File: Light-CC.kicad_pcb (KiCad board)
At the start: 2 copper layers, 69 x 36 mm, 69 parts, among them J1 Conn_01x02_Pin, J2 Conn_01x02_Pin, J3 Conn_01x02_Pin, J4 Conn_01x03_Male, J5 USB_C_Receptacle_USB2.0, Q1 BS870, Q2 STD7NK40Z, Q3 BS870, Q4 BC547, Q5 BC547, Q6 BC547, U1 LM1117-3.3, U2 W25Q64JVSSIQ, U3 RP2040, U4 MIC5219-3.3YM5, Y1 Crystal

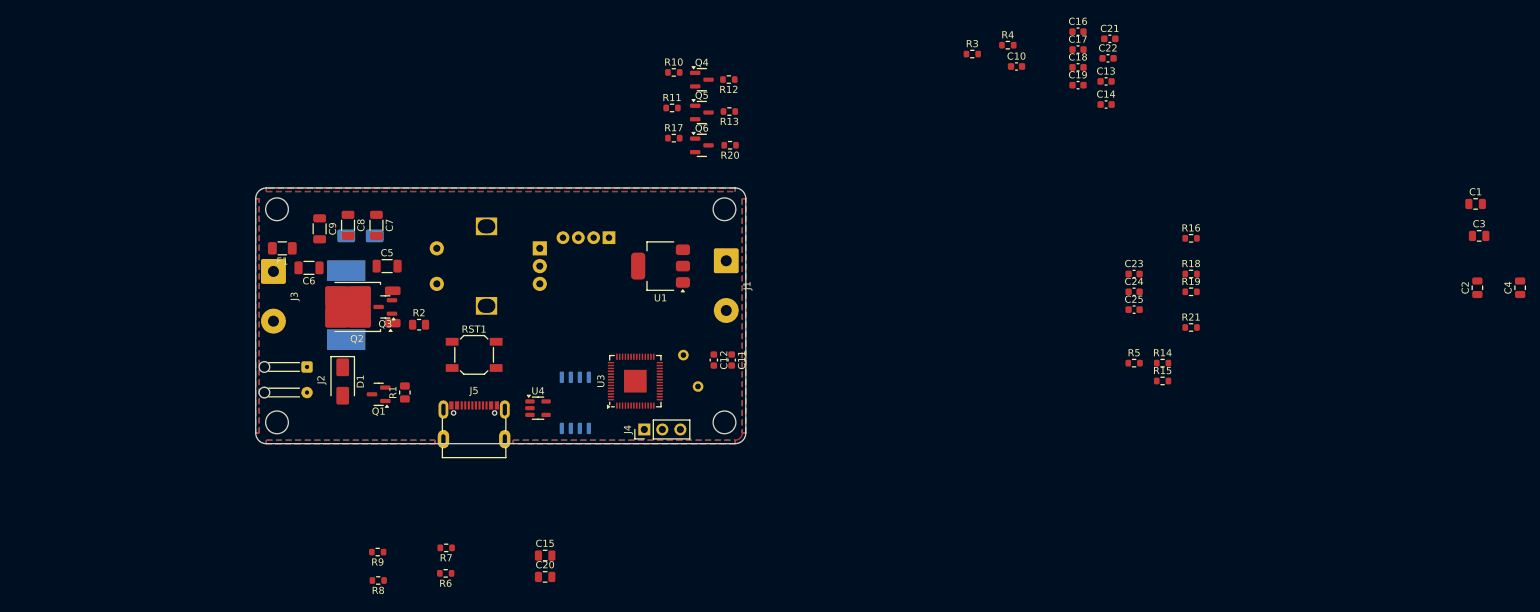
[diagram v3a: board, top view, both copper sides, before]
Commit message: Controller Area placement is done
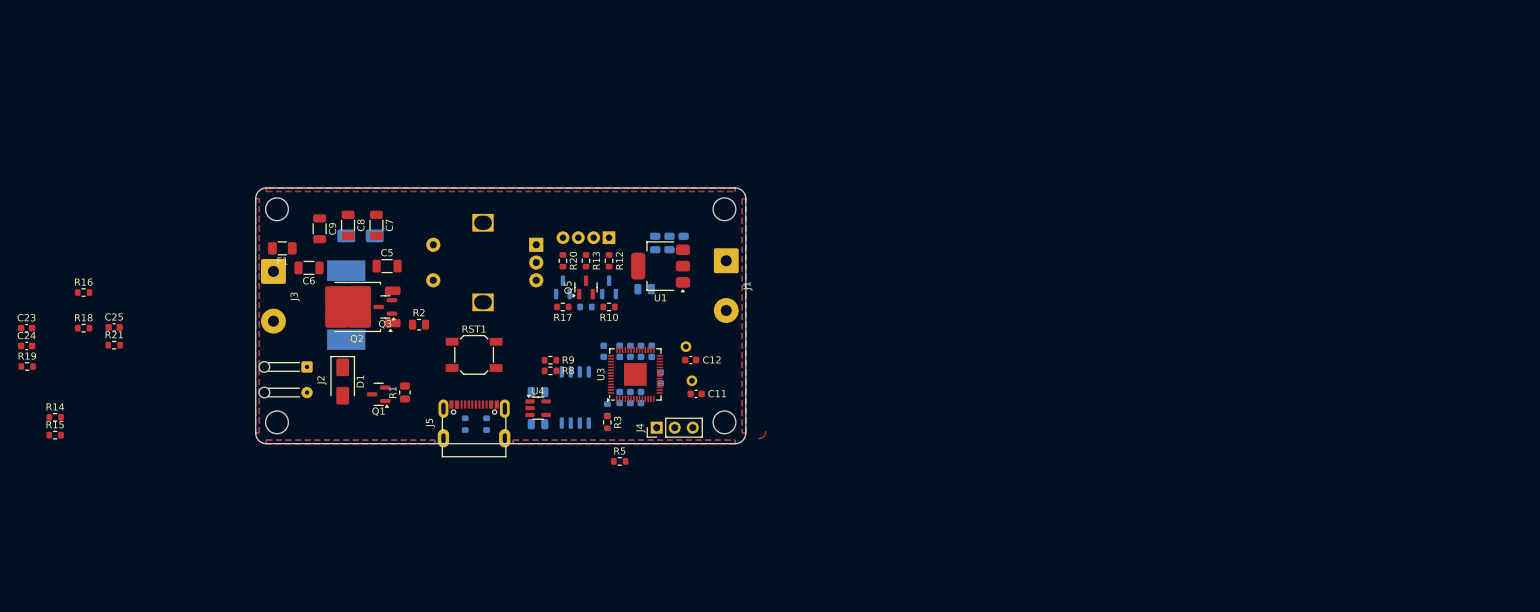
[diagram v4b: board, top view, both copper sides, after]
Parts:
- C1, C10, C13, C14, C15, C16, C17, C18, C19, C2, C20, C21, C22, C3, C4, Q4, Q6, R11, R4, R6, R7: moved to B.Cu
- moved R19 164.2 mm to (47.8, 109.1)
- moved R14 156.1 mm to (51.8, 116.3)
- moved R15 156.1 mm to (51.8, 118.8)
- moved C23 156.1 mm to (47.8, 103.7)
- moved C24 156.1 mm to (47.8, 106.2)
- moved R16 156.1 mm to (55.8, 98.7)
- moved R18 156.1 mm to (55.8, 103.7)
- moved R21 151.6 mm to (60.1, 106.1)
- moved C25 143.6 mm to (60.1, 103.6)
- moved C4 121.9 mm to (136.2, 91.8)
- moved C3 117.7 mm to (134.8, 98.2)
- moved C2 113.9 mm to (138.2, 91.8)
- moved C1 111.6 mm to (140.2, 91.8), turned to 90 degrees
- moved C21 84.3 mm to (132.8, 113.5), turned to 90 degrees
- moved C22 81.3 mm to (134.2, 113.5), turned to 90 degrees
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
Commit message: Layout Routing Beign's
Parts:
- removed MT1: PEC11R-4215F-S0024, Rotary_Encoder:RotaryEncoder_Alps_EC12E-Switch_Vertical_H20mm
- added SW1: RotaryEncoder_Switch, Rotary_Encoder:RotaryEncoder_Alps_EC12E-Switch_Vertical_H20mm, B.Cu at (118.5, 91.5)
- moved R15 69.4 mm to (114.8, 89.8)
- moved C23 68.8 mm to (114.8, 88.0)
- moved R19 68.0 mm to (115.0, 98.2)
- moved R14 67.7 mm to (114.8, 91.5)
- moved C24 67.5 mm to (115.0, 100.0)
- moved R16 59.3 mm to (115.0, 96.5), turned to 180 degrees
- moved R18 51.7 mm to (107.0, 96.5)
- moved R21 47.6 mm to (107.0, 98.2), turned to 180 degrees
- moved C25 47.1 mm to (107.0, 100.0), turned to 180 degrees
- moved U2 1.00 mm to (125.0, 112.5)
- moved RST1 0.75 mm to (110.0, 107.5)
- moved J3 0.35 mm to (82.8, 95.5)
- moved C14 0.28 mm to (137.0, 111.0)
- moved C20 0.25 mm to (119.8, 113.0)
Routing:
- net GND: track 0.00 -> 75.0 mm, vias 0 -> 10
- net +3V3: track 0.00 -> 57.5 mm, vias 0 -> 4
- net /MCU/RE1: track 0.00 -> 34.8 mm
- net /MCU/RE_SW: track 0.00 -> 30.5 mm
- net /MCU/RE2: track 0.00 -> 24.9 mm
- net Net-(U3-VREG_VOUT): track 0.00 -> 23.3 mm, vias 0 -> 2
- net +5V: track 0.00 -> 22.5 mm, vias 0 -> 3
- net /MCU/D+: track 0.00 -> 17.6 mm
- net /MCU/D-: track 0.00 -> 16.9 mm
- net /MCU/LED3: track 0.00 -> 13.1 mm
- net /MCU/SWD: track 0.00 -> 9.46 mm
- net /MCU/SWCLK: track 0.00 -> 9.28 mm
- net /MCU/SD0: track 0.00 -> 9.20 mm, vias 0 -> 1
- net /MCU/SD2: track 0.00 -> 9.06 mm, vias 0 -> 1
- net /MCU/LED2: track 0.00 -> 8.49 mm, vias 0 -> 1
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
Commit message: Layout Routing is 50% complete
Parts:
- C7, C8: footprint Capacitor_SMD:C_1206_3216Metric -> Capacitor_THT:CP_Radial_D5.0mm_P2.50mm
- C9, F1: moved to B.Cu
- D2: moved to F.Cu
- SW1: footprint Rotary_Encoder:RotaryEncoder_Alps_EC12E-Switch_Vertical_H20mm -> Rotary_Encoder:RotaryEncoder_Alps_EC11E_Vertical_H20mm
- moved D1 7.60 mm to (97.8, 116.5), turned to 180 degrees
- moved D2 6.05 mm to (100.8, 90.0), turned to -90 degrees
- moved R2 4.07 mm to (100.2, 106.2)
- moved C8 4.03 mm to (89.0, 88.8)
- moved C9 3.51 mm to (92.5, 90.0)
- moved Q1 2.42 mm to (96.8, 110.7)
- moved J1 2.26 mm to (146.0, 96.5)
- moved R1 2.18 mm to (100.2, 110.8)
- moved RST1 1.35 mm to (108.8, 108.0)
- moved C7 1.33 mm to (95.8, 88.8)
- moved J3 1.03 mm to (82.5, 96.5)
- moved C6 1.00 mm to (88.5, 95.2)
- moved L1 1.00 mm to (93.8, 100.5)
- moved C5 0.56 mm to (99.0, 95.2)
- moved F1 0.56 mm to (84.0, 92.0)
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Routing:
- net +3V3: track 57.5 -> 97.5 mm, vias 4 -> 5
- net /MCU/LED_PWM: track 0.00 -> 38.3 mm
- net /MCU/HAP_PWM: track 0.00 -> 37.8 mm
- net /MCU/SWCLK: track 9.28 -> 29.5 mm
- net /MCU/SWD: track 9.46 -> 26.2 mm
- net GND: track 75.0 -> 90.8 mm, vias 10 -> 12
- net +5V: track 22.5 -> 27.2 mm
- net /MCU/LED3: track 13.1 -> 9.09 mm
- net /MCU/RE_SW: track 30.5 -> 26.7 mm
- net /MCU/LED1: track 6.74 -> 3.24 mm
- net /MCU/RE2: track 24.9 -> 21.4 mm
- net /MCU/LED2: track 8.49 -> 5.49 mm
- net /MCU/RE1: track 34.8 -> 31.8 mm
- added copper zone on B.Cu, net +12V
- added copper zone on F.Cu, net +12V
- added copper zone on B.Cu, net GND
- added copper zone on F.Cu, net GND
- added copper zone on B.Cu, net Net-(D2-A)
- added copper zone on F.Cu, net Net-(D2-A)
- added copper zone on B.Cu, net Net-(J3-Pin_2)
